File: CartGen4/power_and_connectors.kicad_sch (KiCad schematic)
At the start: 33 parts, among them U1 TPS65266-1RHBR

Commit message: Added copyright
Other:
- company: (none) -> © Elijah Almeida Coimbra
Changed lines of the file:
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@@
   (title_block
     (title "Power and connectors")
+    (company "© Elijah Almeida Coimbra")
   )
   (junction (at 120.65 44.45) (diameter 0) (color 0 0 0 0)

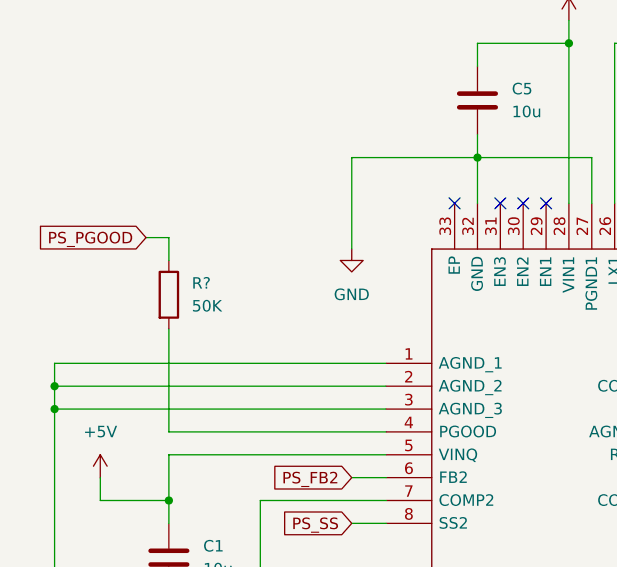
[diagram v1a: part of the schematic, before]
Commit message: Added reference designators to everything
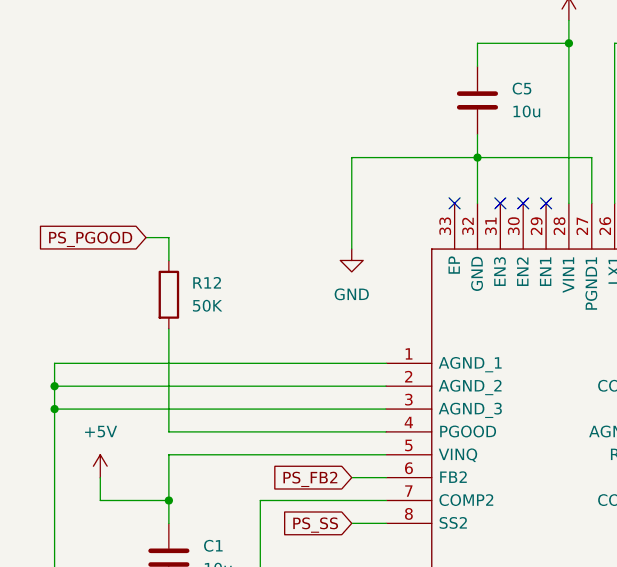
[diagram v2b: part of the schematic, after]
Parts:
- gave numbers to parts that had none: 1
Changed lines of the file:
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@@
   (symbol (lib_id "Device:R") (at 43.18 72.39 0) (unit 1)
     (in_bom yes) (on_board yes) (fields_autoplaced)
-    (property "Reference" "R?" (id 0) (at 45.72 71.1199 0)
+    (property "Reference" "R12" (id 0) (at 45.72 71.1199 0)
       (effects (font (size 1.27 1.27)) (justify left))
     )

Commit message: Fixed DRC
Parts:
- added J2: Conn_01x06_Male, symbol Connector:Conn_01x06_Male
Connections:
- net GND: now also J2.6 (Pin_6)
- net GB_AUDIO: no longer names the net of A1.31 (AUDIO)
- new net FPGA_JTAG_TCK: J2.3 (Pin_3)
- new net FPGA_JTAG_TDI: J2.4 (Pin_4)
- new net FPGA_JTAG_TDO: J2.5 (Pin_5)
- new net FPGA_JTAG_TMS: J2.2 (Pin_2)
- no-connect marks 4 -> 6
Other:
- moved on the sheet: C1, C10, C11, C12, C13, C14, C15, C16, C17, C2, C3, C4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

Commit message: Cleaned up symbol fields
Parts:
- L1, L2, L3: Critical (none) -> Y; MFN (none) -> Murata Electronics; MFP (none) -> DFE252010F-100M=P2; Source (none) -> ANY
- U1: Height 1 -> (none); MFN (none) -> Texas Instruments; MFP (none) -> TPS65266-1RHBR; Manufacturer_Name Texas Instruments -> (none); Manufacturer_Part_Number TPS65266-1RHBR -> (none); Mouser Part Number 595-TPS65266-1RHBR -> (none); Mouser Price/Stock https://www.mouser.co.uk/ProductDetail/Texas-Instruments/TP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 -> (none)
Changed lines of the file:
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@@
       (effects (font (size 1.27 1.27)) hide)
     )
-    (property "Datasheet" "~" (id 3) (at 127 107.95 0)
+    (property "Datasheet" "https://eu.mouser.com/datasheet/2/281/1/J_E_TE243A_0012-2256181.pdf" (id 3) (at 127 107.95 0)
+      (effects (font (size 1.27 1.27)) hide)
+    )
+    (property "Critical" "Y" (id 4) (at 127 107.95 0)
+      (effects (font (size 1.27 1.27)) hide)
+    )
+    (property "MFN" "Murata Electronics" (id 5) (at 127 107.95 0)
+      (effects (font (size 1.27 1.27)) hide)
+    )
+    (property "MFP" "DFE252010F-100M=P2" (id 6) (at 127 107.95 0)
+      (effects (font (size 1.27 1.27)) hide)
+    )
+    (property "Source" "ANY" (id 7) (at 127 107.95 0)
       (effects (font (size 1.27 1.27)) hide)
     )
@@
       (effects (font (size 1.27 1.27)) hide)
     )
-    (property "Datasheet" "~" (id 3) (at 83.82 139.7 0)
+    (property "Datasheet" "https://eu.mouser.com/datasheet/2/281/1/J_E_TE243A_0012-2256181.pdf" (id 3) (at 83.82 139.7 0)
+      (effects (font (size 1.27 1.27)) hide)
+    )
+    (property "MFN" "Murata Electronics" (id 4) (at 83.82 139.7 90)
+      (effects (font (size 1.27 1.27)) hide)
+    )
+    (property "MFP" "DFE252010F-100M=P2" (id 5) (at 83.82 139.7 90)
+      (effects (font (size 1.27 1.27)) hide)
+    )
+    (property "Package ID" "" (id 6) (at 83.82 139.7 90)
+      (effects (font (size 1.27 1.27)) hide)
+    )
+    (property "Source" "ANY" (id 7) (at 83.82 139.7 90)
+      (effects (font (size 1.27 1.27)) hide)
+    )
+    (property "Critical" "Y" (id 8) (at 83.82 139.7 90)
+      (effects (font (size 1.27 1.27)) hide)
+    )
+    (property "Notes" "" (id 9) (at 83.82 139.7 90)
       (effects (font (size 1.27 1.27)) hide)
     )
@@
       (effects (font (size 1.27 1.27)) (justify left) hide)
     )
-    (property "Height" "1" (id 5) (at 99.06 62.23 0)
+    (property "MFN" "Texas Instruments" (id 5) (at 99.06 69.85 0)
       (effects (font (size 1.27 1.27)) (justify left) hide)
     )
-    (property "Mouser Part Number" "595-TPS65266-1RHBR" (id 6) (at 99.06 64.77 0)
-      (effects (font (size 1.27 1.27)) (justify left) hide)
-    )
-    (property "Mouser Price/Stock" "https://www.mouser.co.uk/ProductDetail/Texas-Instruments/TPS65266-1RHBR?qs=8N88piwwHEiYjq5W9uWjdA%3D%3D" (id 7) (at 99.06 67.31 0)
-      (effects (font (size 1.27 1.27)) (justify left) hide)
-    )
-    (property "Manufacturer_Name" "Texas Instruments" (id 8) (at 99.06 69.85 0)
-      (effects (font (size 1.27 1.27)) (justify left) hide)
-    )
-    (property "Manufacturer_Part_Number" "TPS65266-1RHBR" (id 9) (at 99.06 72.39 0)
+    (property "MFP" "TPS65266-1RHBR" (id 6) (at 99.06 72.39 0)
       (effects (font (size 1.27 1.27)) (justify left) hide)
     )
@@
       (effects (font (size 1.27 1.27)) hide)
     )
-    (property "Datasheet" "~" (id 3) (at 104.14 31.75 0)
-      (effects (font (size 1.27 1.27)) hide)
-    )
+    (property "Datasheet" "https://eu.mouser.com/datasheet/2/281/1/J_E_TE243A_0012-2256181.pdf" (id 3) (at 104.14 31.75 0)
+      (effects (font (size 1.27 1.27)) hide)
+    )
+    (property "Critical" "Y" (id 4) (at 104.14 31.75 0)
+      (effects (font (size 1.27 1.27)) hide)
+    )
+    (property "MFN" "Murata Electronics" (id 5) (at 104.14 31.75 0)
+      (effects (font (size 1.27 1.27)) hide)
+    )
+    (property "MFP" "DFE252010F-100M=P2" (id 6) (at 104.14 31.75 0)
+      (effects (font (size 1.27 1.27)) hide)
+    )
+    (property "Source" "ANY" (id 7) (at 104.14 31.75 0)
+      (effects (font (size 1.27 1.27)) hide)
+    )

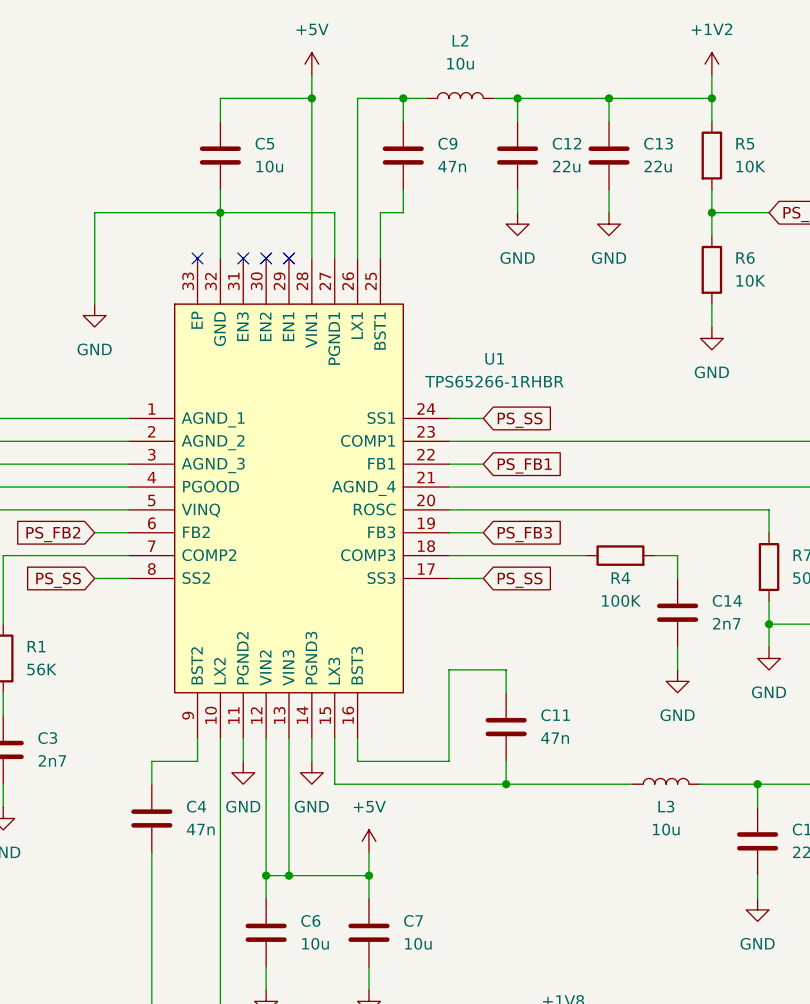
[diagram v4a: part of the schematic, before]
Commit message: Added symbol information to obvious stuff
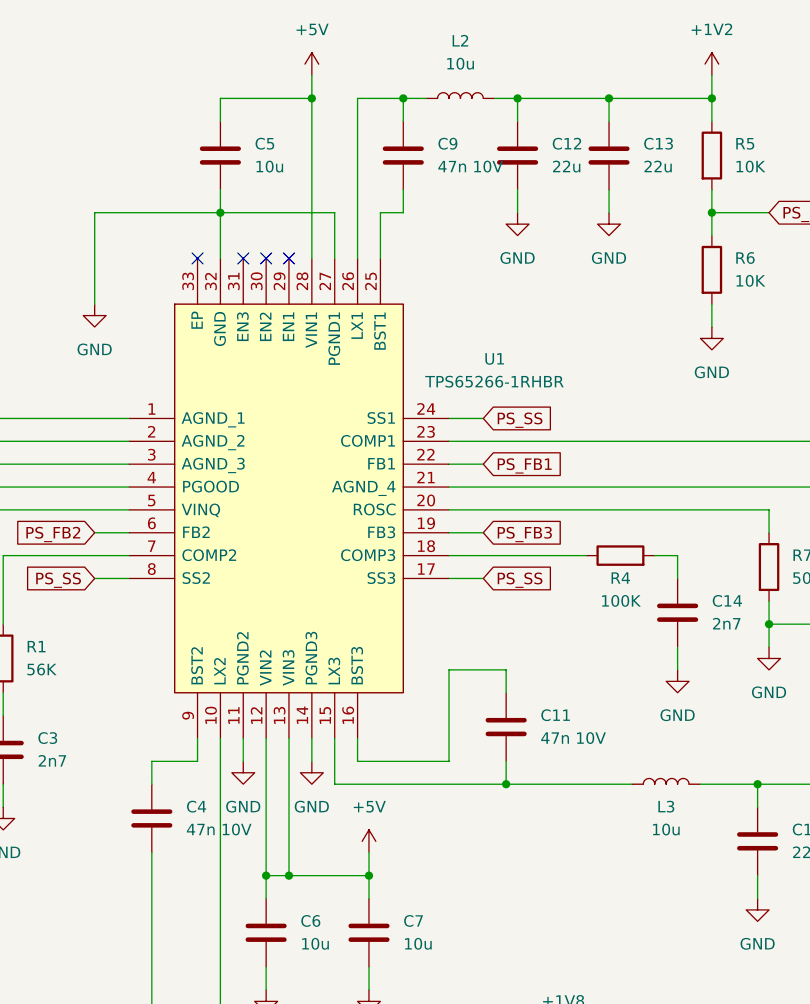
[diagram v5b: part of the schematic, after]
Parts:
- A1: Critical (none) -> Y
- C1, C5, C6, C7: Critical (none) -> Y; Notes (none) -> Used for filtering of the power supply input.
- C10, C12, C13, C15, C16, C8: Critical (none) -> Y; Notes (none) -> Used for filtering of the power supply output.
- C11, C4, C9: value 47n -> 47n 10V; Critical (none) -> Y; Notes (none) -> Bootstrap capacitor for SMPS. Value is recommended by the d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
- C2: Critical (none) -> N; Notes (none) -> Used for soft start of the power supply. Since no component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
- U1: Critical (none) -> Y; Notes (none) -> Switched mode power supply for generating the required powe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; Package ID (none) -> VQFN-32; Source (none) -> SPEC
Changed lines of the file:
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@@
       (effects (font (size 1.27 1.27)) (justify left))
     )
-    (property "Value" "47n" (id 1) (at 73.66 113.0299 0)
+    (property "Value" "47n 10V" (id 1) (at 73.66 113.0299 0)
       (effects (font (size 1.27 1.27)) (justify left))
     )
@@
     )
     (property "Datasheet" "~" (id 3) (at 69.85 111.76 0)
+      (effects (font (size 1.27 1.27)) hide)
+    )
+    (property "Critical" "Y" (id 4) (at 69.85 111.76 0)
+      (effects (font (size 1.27 1.27)) hide)
+    )
+    (property "Notes" "Bootstrap capacitor for SMPS. Value is recommended by the datasheet." (id 5) (at 69.85 111.76 0)
       (effects (font (size 1.27 1.27)) hide)
     )
@@
       (effects (font (size 1.27 1.27)) (justify left))
     )
-    (property "Value" "47n" (id 1) (at 113.03 102.8699 0)
+    (property "Value" "47n 10V" (id 1) (at 113.03 102.8699 0)
       (effects (font (size 1.27 1.27)) (justify left))
     )
@@
     )
     (property "Datasheet" "~" (id 3) (at 109.22 101.6 0)
+      (effects (font (size 1.27 1.27)) hide)
+    )
+    (property "Critical" "Y" (id 4) (at 109.22 101.6 0)
+      (effects (font (size 1.27 1.27)) hide)
+    )
+    (property "Notes" "Bootstrap capacitor for SMPS. Value is recommended by the datasheet." (id 5) (at 109.22 101.6 0)
       (effects (font (size 1.27 1.27)) hide)
     )
@@
       (effects (font (size 1.27 1.27)) hide)
     )
-    (property "Datasheet" "" (id 3) (at 271.78 62.23 0)
+    (property "Datasheet" "~" (id 3) (at 271.78 62.23 0)
+      (effects (font (size 1.27 1.27)) hide)
+    )
+    (property "Critical" "Y" (id 4) (at 271.78 101.6 0)
+      (effects (font (size 1.27 1.27)) hide)
+    )
+    (property "Description" "Board outline for a Gameboy cartridge" (id 5) (at 271.78 101.6 0)
+      (effects (font (size 1.27 1.27)) hide)
+    )
+    (property "MFN" "~" (id 6) (at 271.78 101.6 0)
+      (effects (font (size 1.27 1.27)) hide)
+    )
+    (property "MFP" "~" (id 7) (at 271.78 101.6 0)
+      (effects (font (size 1.27 1.27)) hide)
+    )
+    (property "Notes" "~" (id 8) (at 271.78 101.6 0)
+      (effects (font (size 1.27 1.27)) hide)
+    )
+    (property "Package ID" "~" (id 9) (at 271.78 101.6 0)
+      (effects (font (size 1.27 1.27)) hide)
+    )
+    (property "Source" "~" (id 10) (at 271.78 101.6 0)
       (effects (font (size 1.27 1.27)) hide)
     )
@@
       (effects (font (size 1.27 1.27)) hide)
     )
+    (property "Critical" "N" (id 4) (at 43.18 132.08 0)
+      (effects (font (size 1.27 1.27)) hide)
+    )
+    (property "Notes" "Used for soft start of the power supply. Since no component has a specific startup sequence, it really doesn't matter what the value is, as long as it isn't too large since that increases startup time." (id 5) (at 43.18 132.08 0)
+      (effects (font (size 1.27 1.27)) hide)
+    )
     (pin "1")
     (pin "2")
@@
     )
     (property "Datasheet" "~" (id 3) (at 110.49 38.1 0)
+      (effects (font (size 1.27 1.27)) hide)
+    )
+    (property "Critical" "Y" (id 4) (at 110.49 38.1 0)
+      (effects (font (size 1.27 1.27)) hide)
+    )
+    (property "Notes" "Used for filtering of the power supply output." (id 5) (at 110.49 38.1 0)
       (effects (font (size 1.27 1.27)) hide)
     )
@@
       (effects (font (size 1.27 1.27)) hide)
     )
+    (property "Critical" "Y" (id 4) (at 148.59 114.3 0)
+      (effects (font (size 1.27 1.27)) hide)
+    )
+    (property "Notes" "Used for filtering of the power supply output." (id 5) (at 148.59 114.3 0)
+      (effects (font (size 1.27 1.27)) hide)
+    )
     (pin "1")
     (pin "2")
@@
       (effects (font (size 1.27 1.27)) hide)
     )
+    (property "Critical" "Y" (id 4) (at 93.98 124.46 0)
+      (effects (font (size 1.27 1.27)) hide)
+    )
+    (property "Notes" "Used for filtering of the power supply input." (id 5) (at 93.98 124.46 0)
+      (effects (font (size 1.27 1.27)) hide)
+    )
     (pin "1")
     (pin "2")
@@
     )
     (property "Datasheet" "~" (id 3) (at 82.55 124.46 0)
+      (effects (font (size 1.27 1.27)) hide)
+    )
+    (property "Critical" "Y" (id 4) (at 82.55 124.46 0)
+      (effects (font (size 1.27 1.27)) hide)
+    )
+    (property "Notes" "Used for filtering of the power supply input." (id 5) (at 82.55 124.46 0)
       (effects (font (size 1.27 1.27)) hide)
     )
@@
       (effects (font (size 1.27 1.27)) hide)
     )
+    (property "Critical" "Y" (id 4) (at 105.41 146.05 0)
+      (effects (font (size 1.27 1.27)) hide)
+    )
+    (property "Notes" "Used for filtering of the power supply output." (id 5) (at 105.41 146.05 0)
+      (effects (font (size 1.27 1.27)) hide)
+    )
     (pin "1")
     (pin "2")
@@
     )
     (property "Datasheet" "~" (id 3) (at 137.16 114.3 0)
+      (effects (font (size 1.27 1.27)) hide)
+    )
+    (property "Critical" "Y" (id 4) (at 137.16 114.3 0)
+      (effects (font (size 1.27 1.27)) hide)
+    )
+    (property "Notes" "Used for filtering of the power supply output." (id 5) (at 137.16 114.3 0)
       (effects (font (size 1.27 1.27)) hide)
     )
@@
     (property "MFP" "TPS65266-1RHBR" (id 6) (at 99.06 72.39 0)
       (effects (font (size 1.27 1.27)) (justify left) hide)
+    )
+    (property "Notes" "Switched mode power supply for generating the required power lines (1V2, 1V8 and 3V3)." (id 7) (at 67.31 67.31 0)
+      (effects (font (size 1.27 1.27)) hide)
+    )
+    (property "Package ID" "VQFN-32" (id 8) (at 67.31 67.31 0)
+      (effects (font (size 1.27 1.27)) hide)
+    )
+    (property "Source" "SPEC" (id 9) (at 67.31 67.31 0)
+      (effects (font (size 1.27 1.27)) hide)
+    )
+    (property "Critical" "Y" (id 10) (at 67.31 67.31 0)
+      (effects (font (size 1.27 1.27)) hide)
     )
     (pin "1")
@@
       (effects (font (size 1.27 1.27)) hide)
     )
+    (property "Critical" "Y" (id 4) (at 77.47 38.1 0)
+      (effects (font (size 1.27 1.27)) hide)
+    )
+    (property "Notes" "Used for filtering of the power supply input." (id 5) (at 77.47 38.1 0)
+      (effects (font (size 1.27 1.27)) hide)
+    )
     (pin "1")
     (pin "2")
@@
       (effects (font (size 1.27 1.27)) hide)
     )
+    (property "Critical" "Y" (id 4) (at 120.65 38.1 0)
+      (effects (font (size 1.27 1.27)) hide)
+    )
+    (property "Notes" "Used for filtering of the power supply output." (id 5) (at 120.65 38.1 0)
+      (effects (font (size 1.27 1.27)) hide)
+    )
     (pin "1")
     (pin "2")
@@
     )
     (property "Datasheet" "~" (id 3) (at 93.98 146.05 0)
+      (effects (font (size 1.27 1.27)) hide)
+    )
+    (property "Critical" "Y" (id 4) (at 93.98 146.05 0)
+      (effects (font (size 1.27 1.27)) hide)
+    )
+    (property "Notes" "Used for filtering of the power supply output." (id 5) (at 93.98 146.05 0)
       (effects (font (size 1.27 1.27)) hide)
     )
@@
       (effects (font (size 1.27 1.27)) (justify left))
     )
-    (property "Value" "47n" (id 1) (at 101.6 39.3699 0)
+    (property "Value" "47n 10V" (id 1) (at 101.6 39.3699 0)
       (effects (font (size 1.27 1.27)) (justify left))
     )
@@
     )
     (property "Datasheet" "~" (id 3) (at 97.79 38.1 0)
+      (effects (font (size 1.27 1.27)) hide)
+    )
+    (property "Critical" "Y" (id 4) (at 97.79 38.1 0)
+      (effects (font (size 1.27 1.27)) hide)
+    )
+    (property "Notes" "Bootstrap capacitor for SMPS. Value is recommended by the datasheet." (id 5) (at 97.79 38.1 0)
       (effects (font (size 1.27 1.27)) hide)
     )
@@
       (effects (font (size 1.27 1.27)) hide)
     )
+    (property "Critical" "Y" (id 4) (at 43.18 88.9 0)
+      (effects (font (size 1.27 1.27)) hide)
+    )
+    (property "Notes" "Used for filtering of the power supply input." (id 5) (at 43.18 88.9 0)
+      (effects (font (size 1.27 1.27)) hide)
+    )

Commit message: Added more symbol information
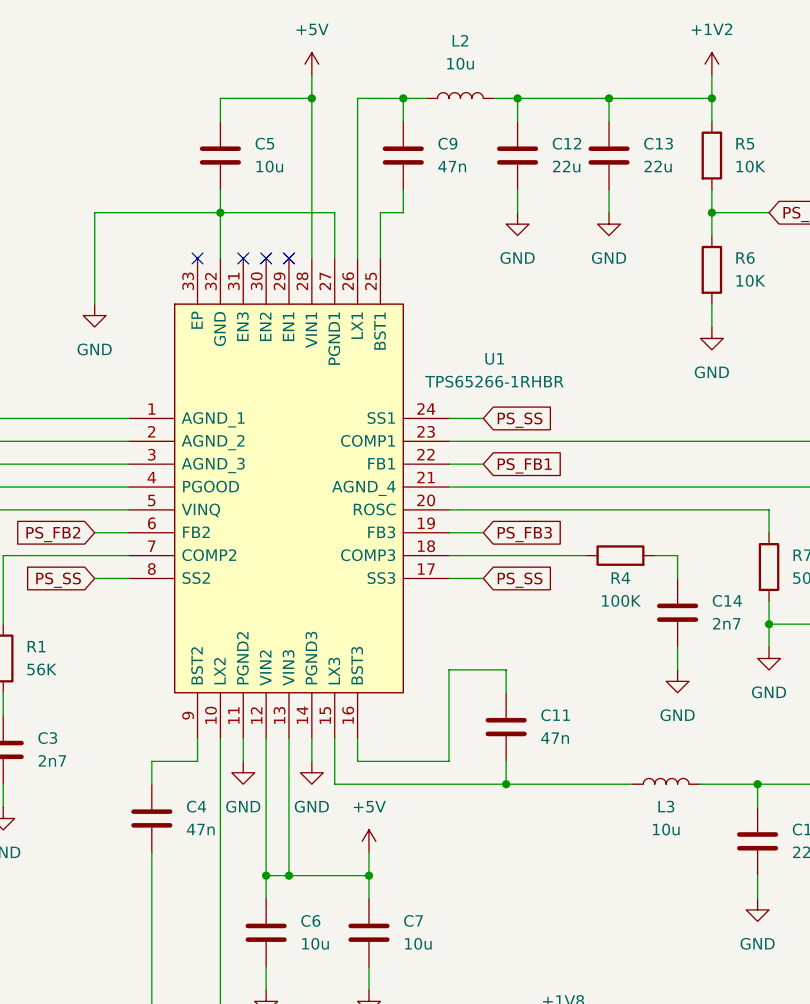
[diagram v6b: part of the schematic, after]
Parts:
- C1, C5, C6, C7: Current (none) -> 500mA; Notes Used for filtering of the power supply input. -> Used for filtering of the power supply input. Recommended X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; Source (none) -> ANY; Voltage (none) -> 10V
- C10, C12, C13, C15, C16, C8: Current (none) -> 35mA; ESR (none) -> 107m; Source (none) -> ANY
- C11, C4, C9: value 47n 10V -> 47n; Notes Bootstrap capacitor for SMPS. Value is recommended by the datasheet. -> Bootstrap capacitor for SMPS. Value is recommended by the datasheet. Recommended X5R or X7R dielectric.; Source (none) -> ANY; Voltage (none) -> 10V
- C14, C17, C3: Critical (none) -> Y
- C2: Source (none) -> ANY
- J2: Critical (none) -> N; Notes (none) -> Connector for getting access to JTAG.; Source (none) -> ANY
- L1, L2, L3: Current (none) -> 500mA; Tolerance (none) -> 20%
- R1, R12, R4, R7, R8: Critical (none) -> Y; Source (none) -> ANY; Tolerance (none) -> 10%
- R10, R2, R3, R5, R6, R9: Critical (none) -> Y; Source (none) -> ANY; Tolerance (none) -> 1%

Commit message: Converted footprints
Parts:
- U1: footprint QFN50P500X500X100-33N-D -> SamacSys_Parts:QFN50P500X500X100-33N-D
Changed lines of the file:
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@@
     (property "Reference" "U1" (id 0) (at 107.95 60.7312 0))
     (property "Value" "TPS65266-1RHBR" (id 1) (at 107.95 63.2712 0))
-    (property "Footprint" "QFN50P500X500X100-33N-D" (id 2) (at 99.06 54.61 0)
+    (property "Footprint" "SamacSys_Parts:QFN50P500X500X100-33N-D" (id 2) (at 99.06 54.61 0)
       (effects (font (size 1.27 1.27)) (justify left) hide)
     )
